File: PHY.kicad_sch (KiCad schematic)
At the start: 0 parts

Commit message: design CPU-RK3399 eMMC Controller
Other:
- company: (none) -> TickLab
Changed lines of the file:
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@@
 	(paper "A4")
 	(title_block
-		(date "2026-01-09")
+		(date "2026-01-14")
 		(rev "1.0.0")
+		(company "TickLab")
 	)
 	(bus_alias "PHY_MDI"

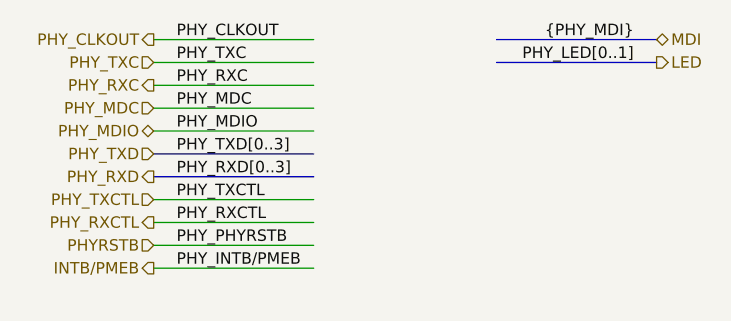
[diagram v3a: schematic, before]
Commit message: update schematic
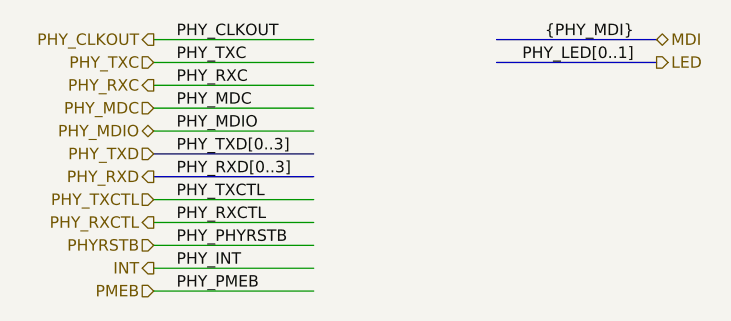
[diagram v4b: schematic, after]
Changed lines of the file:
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@@
 		(rev "1.0.0")
 		(company "TickLab")
+		(comment 1 "Project: VESA-SBC3399")
 	)
 	(bus_alias "PHY_MDI"
@@
 	(wire
 		(pts
+			(xy 116.84 119.38) (xy 134.62 119.38)
+		)
+		(stroke
+			(width 0)
+			(type default)
+		)
+	)
+	(wire
+		(pts
 			(xy 116.84 101.6) (xy 134.62 101.6)
 		)
@@
 		)
 	)
+	(label "PHY_PMEB"
+		(at 119.38 119.38 0)
+		(effects
+			(font
+				(size 1.27 1.27)
+			)
+			(justify left bottom)
+		)
+	)
 	(label "PHY_MDIO"
 		(at 119.38 101.6 0)
@@
 		)
 	)
-	(label "PHY_INTB{slash}PMEB"
+	(label "PHY_INT"
 		(at 119.38 116.84 0)
 		(effects
@@
 		)
 	)
-	(hierarchical_label "INTB{slash}PMEB"
+	(hierarchical_label "INT"
 		(shape output)
 		(at 116.84 116.84 180)
@@
 		(effects
 			(font
+				(size 1.27 1.27)
+			)
+			(justify right)
+		)
+	)
+	(hierarchical_label "PMEB"
+		(shape input)
+		(at 116.84 119.38 180)
+		(effects
+			(font
